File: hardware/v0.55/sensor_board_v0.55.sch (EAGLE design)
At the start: 61 parts, among them J3 USB-MICROB, J6 AVR_SPI_PRG_6PTH, U1 ATMEGA328P, U10 TSL2591, U11 915MHz, U2 SHT35, U3 OPA344, U5 FT231XS, U6 ADMP401, U7 PMS7003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

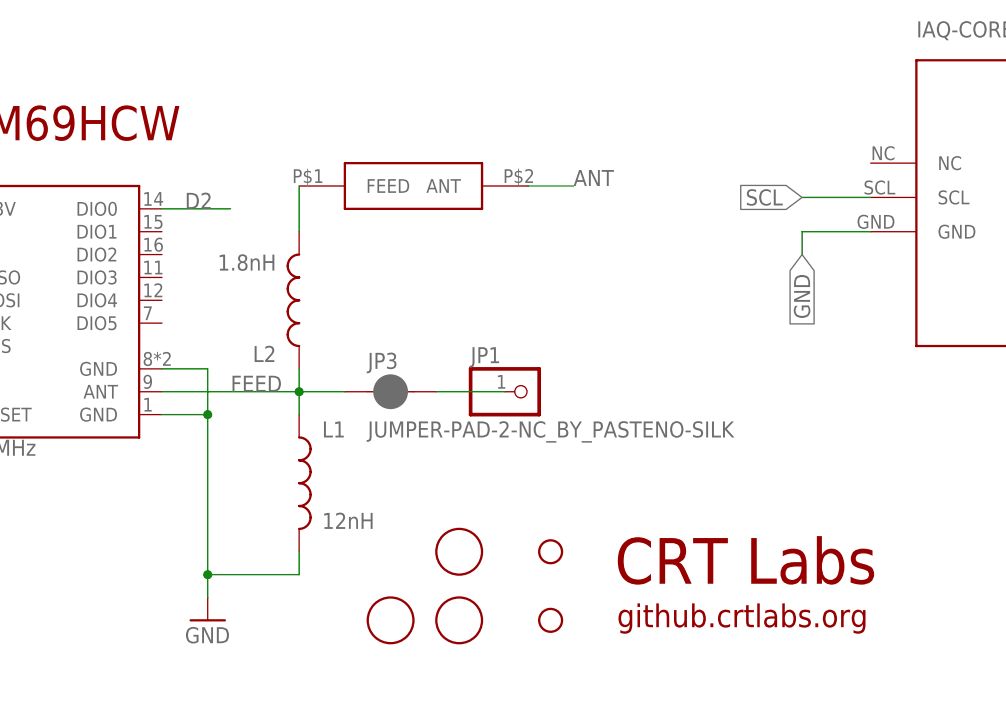
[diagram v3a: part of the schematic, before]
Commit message: Redesigned antenna trace
- Removed trace for wire monopole (it needs GND plane underneath, so
wouldn't have worked anyway)
- Added jumper for SMD feed (if chip doesn't work, remove jumper, solder
wire monopole directly to radio ANT pad
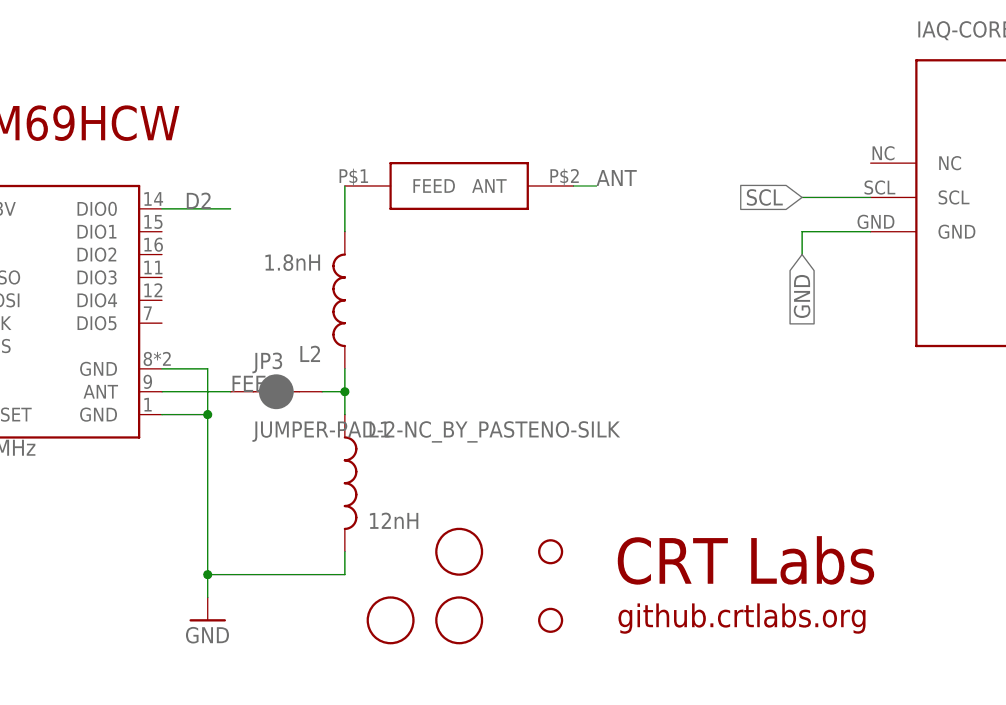
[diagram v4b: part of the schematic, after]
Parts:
- removed JP1: (no value), adafruit:PINHD-1X1
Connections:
- net FEED: now also JP3.2; no longer JP3.1, U11.ANT
- net N$6: now also JP3.1, U11.ANT; no longer JP1.1, JP3.2
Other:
- moved on the sheet: JP3, L1, L2
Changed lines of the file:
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@@
 <part name="L1" library="SparkFun-Passives" deviceset="INDUCTOR" device="0805-IND" value="12nH"/>
 <part name="L2" library="SparkFun-Passives" deviceset="INDUCTOR" device="0805-IND" value="1.8nH"/>
-<part name="JP1" library="adafruit" deviceset="PINHD-1X1" device=""/>
 <part name="JP3" library="SparkFun-Passives" deviceset="JUMPER-PAD-2-NC_BY_PASTE" device="NO-SILK"/>
 </parts>
@@
 <attribute name="MPN" x="106.68" y="-68.58" size="1.778" layer="96" rot="R90" display="off"/>
 </instance>
-<instance part="U$4" gate="G$1" x="170.18" y="-58.42"/>
-<instance part="L1" gate="G$1" x="157.48" y="-91.44"/>
-<instance part="L2" gate="G$1" x="157.48" y="-71.12" rot="R180"/>
-<instance part="JP1" gate="G$1" x="182.88" y="-81.28"/>
-<instance part="JP3" gate="G$1" x="167.64" y="-81.28"/>
+<instance part="U$4" gate="G$1" x="175.26" y="-58.42"/>
+<instance part="L1" gate="G$1" x="162.56" y="-91.44"/>
+<instance part="L2" gate="G$1" x="162.56" y="-71.12" rot="R180"/>
+<instance part="JP3" gate="G$1" x="154.94" y="-81.28"/>
 </instances>
 <busses>
@@
 <pinref part="GND5" gate="1" pin="GND"/>
 <pinref part="L1" gate="G$1" pin="2"/>
-<wire x1="147.32" y1="-101.6" x2="157.48" y2="-101.6" width="0.1524" layer="91"/>
-<wire x1="157.48" y1="-101.6" x2="157.48" y2="-99.06" width="0.1524" layer="91"/>
+<wire x1="147.32" y1="-101.6" x2="162.56" y2="-101.6" width="0.1524" layer="91"/>
+<wire x1="162.56" y1="-101.6" x2="162.56" y2="-99.06" width="0.1524" layer="91"/>
 <junction x="147.32" y="-101.6"/>
 </segment>
@@
 <net name="FEED" class="0">
 <segment>
-<pinref part="U11" gate="G$1" pin="ANT"/>
-<wire x1="142.24" y1="-81.28" x2="157.48" y2="-81.28" width="0.1524" layer="91"/>
 <label x="149.86" y="-81.28" size="1.778" layer="95"/>
 <pinref part="L2" gate="G$1" pin="1"/>
-<wire x1="157.48" y1="-78.74" x2="157.48" y2="-81.28" width="0.1524" layer="91"/>
 <pinref part="L1" gate="G$1" pin="1"/>
-<wire x1="157.48" y1="-81.28" x2="157.48" y2="-83.82" width="0.1524" layer="91"/>
-<junction x="157.48" y="-81.28"/>
-<wire x1="157.48" y1="-81.28" x2="162.56" y2="-81.28" width="0.1524" layer="91"/>
-<pinref part="JP3" gate="G$1" pin="1"/>
+<wire x1="162.56" y1="-78.74" x2="162.56" y2="-81.28" width="0.1524" layer="91"/>
+<pinref part="JP3" gate="G$1" pin="2"/>
+<wire x1="162.56" y1="-81.28" x2="162.56" y2="-83.82" width="0.1524" layer="91"/>
+<wire x1="160.02" y1="-81.28" x2="162.56" y2="-81.28" width="0.1524" layer="91"/>
+<junction x="162.56" y="-81.28"/>
 </segment>
 </net>
@@
 <net name="ANT" class="0">
 <segment>
-<wire x1="182.88" y1="-58.42" x2="187.96" y2="-58.42" width="0.1524" layer="91"/>
-<label x="187.96" y="-58.42" size="1.778" layer="95"/>
+<wire x1="187.96" y1="-58.42" x2="190.5" y2="-58.42" width="0.1524" layer="91"/>
+<label x="190.5" y="-58.42" size="1.778" layer="95"/>
 <pinref part="U$4" gate="G$1" pin="ANT"/>
 </segment>
@@
 <pinref part="L2" gate="G$1" pin="2"/>
 <pinref part="U$4" gate="G$1" pin="FEED"/>
-<wire x1="157.48" y1="-63.5" x2="157.48" y2="-58.42" width="0.1524" layer="91"/>
+<wire x1="162.56" y1="-63.5" x2="162.56" y2="-58.42" width="0.1524" layer="91"/>
 </segment>
 </net>
 <net name="N$6" class="0">
 <segment>
-<pinref part="JP1" gate="G$1" pin="1"/>
-<wire x1="172.72" y1="-81.28" x2="180.34" y2="-81.28" width="0.1524" layer="91"/>
-<pinref part="JP3" gate="G$1" pin="2"/>
-</segment>
-</net>
+<pinref part="U11" gate="G$1" pin="ANT"/>
+<pinref part="JP3" gate="G$1" pin="1"/>
+<wire x1="142.24" y1="-81.28" x2="149.86" y2="-81.28" width="0.1524" layer="91"/>
+</segment>
+</net>
